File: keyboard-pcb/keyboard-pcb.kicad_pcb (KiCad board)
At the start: 2 copper layers, 57 parts, among them SW1 SW_Push, SW10 SW_Push, SW11 SW_Push, SW12 SW_Push, SW13 SW_Push, SW14 SW_Push, SW15 SW_Push, SW16 SW_Push, SW17 SW_Push, SW18 SW_Push, SW19 SW_Push, SW2 SW_Push, SW20 SW_Push, SW21 SW_Push, SW22 SW_Push, SW23 SW_Push, SW24 SW_Push, SW25 SW_Push, SW26 SW_Push, SW27 SW_Push, SW28 SW_Push, SW3 SW_Push, SW4 SW_Push, SW5 SW_Push, SW6 SW_Push, SW7 SW_Push, SW8 SW_Push, SW9 SW_Push, U1 RC1602A

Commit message: placement in progress
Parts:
- removed D28: 1N914, Diode_THT:D_DO-35_SOD27_P7.62mm_Horizontal
- removed SW28: SW_Push, Button_Switch_Keyboard:SW_Cherry_MX_1.00u_PCB
- added U1: ATmega328-P, Package_DIP:DIP-28_W7.62mm, F.Cu at (215.9, 52.1)
- D16, D20, D23, D7: moved to B.Cu
- moved SW24 169.6 mm to (102.9, 158.8)
- moved SW27 161.3 mm to (93.5, 178.4)
- moved D20 147.5 mm to (104.1, 154.3), turned to 180 degrees
- moved D23 146.3 mm to (85.1, 172.7), turned to 180 degrees
- moved SW22 146.3 mm to (64.8, 158.8)
- moved D16 140.7 mm to (104.1, 135.3), turned to 180 degrees
- moved SW26 126.6 mm to (64.8, 177.8)
- moved D7 123.0 mm to (85.1, 97.2), turned to 180 degrees
- moved SW23 122.6 mm to (83.8, 158.8)
- moved SW25 117.2 mm to (45.7, 177.8)
- renumbered U1 to U2
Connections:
- net Net-(D1-K) renamed /COL0
- net Net-(D10-K) renamed /COL1
- net Net-(D11-K) renamed /COL2
- net Net-(D12-K) renamed /COL3
- net Net-(SW1-Pad1) renamed /ROW0
- net Net-(SW10-Pad1) renamed /ROW2
- net Net-(SW13-Pad1) renamed /ROW3
- net Net-(SW17-Pad1) renamed /ROW4
- net Net-(SW21-Pad1) renamed /ROW5
- net Net-(SW25-Pad1) renamed /ROW6
- net Net-(SW5-Pad1) renamed /ROW1
- U2 pad 1: unconnected-(U1-VSS-Pad1) -> GND
- U2 pad 2: unconnected-(U1-VDD-Pad2) -> VCC
- U2 pad 5: unconnected-(U1-R/W-Pad5) -> GND

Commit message: placement
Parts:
- added R1: R, Resistor_THT:R_Axial_DIN0207_L6.3mm_D2.5mm_P7.62mm_Horizontal, B.Cu at (52.1, 53.3)
- added RV1: R_Potentiometer, Potentiometer_THT:Potentiometer_Bourns_3266P_Horizontal, B.Cu at (35.6, 40.6)
- U1: moved to B.Cu
- moved U1 128.7 mm to (87.6, 41.9), turned to 90 degrees
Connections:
- U2 pad 10: unconnected-(U2-DB3-Pad10) -> GND
- U2 pad 11: unconnected-(U2-DB4-Pad11) -> /D0
- U2 pad 12: unconnected-(U2-DB5-Pad12) -> /D1
- U2 pad 13: unconnected-(U2-DB6-Pad13) -> /D2
- U2 pad 14: unconnected-(U2-DB7-Pad14) -> /D3
- U2 pad 15: unconnected-(U2-A/VEE-Pad15) -> VCC
- U2 pad 16: unconnected-(U2-K-Pad16) -> Net-(U2-K)
- U2 pad 3: unconnected-(U2-VO-Pad3) -> Net-(U2-VO)
- U2 pad 4: unconnected-(U2-RS-Pad4) -> /RS
- U2 pad 6: unconnected-(U2-E-Pad6) -> /EN
- U2 pad 7: unconnected-(U2-DB0-Pad7) -> GND
- U2 pad 8: unconnected-(U2-DB1-Pad8) -> GND
- U2 pad 9: unconnected-(U2-DB2-Pad9) -> GND

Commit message: working on placement
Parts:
- added C1: 0.1uF, Capacitor_SMD:C_0805_2012Metric_Pad1.18x1.45mm_HandSolder, F.Cu at (129.3, 96.7)
- added C2: 10uF, Capacitor_SMD:C_0805_2012Metric_Pad1.18x1.45mm_HandSolder, F.Cu at (129.3, 99.7)
- added C3: 0.1uF, Capacitor_SMD:C_0805_2012Metric_Pad1.18x1.45mm_HandSolder, F.Cu at (129.3, 102.7)
- added D1: LED, LED_THT:LED_D3.0mm, F.Cu at (122.7, 81.7)
- added D11: LED, LED_THT:LED_D3.0mm, F.Cu at (122.7, 92.8)
- added D2: LED, LED_THT:LED_D3.0mm, F.Cu at (122.7, 87.3)
- added J1: Conn_02x03_Odd_Even, Connector_PinHeader_2.54mm:PinHeader_2x03_P2.54mm_Vertical, F.Cu at (140.0, 81.3)
- added R1: 470, Resistor_THT:R_Axial_DIN0207_L6.3mm_D2.5mm_P7.62mm_Horizontal, F.Cu at (128.5, 81.0)
- added R2: 470, Resistor_THT:R_Axial_DIN0207_L6.3mm_D2.5mm_P7.62mm_Horizontal, F.Cu at (128.5, 85.0)
- added R3: 470, Resistor_THT:R_Axial_DIN0207_L6.3mm_D2.5mm_P7.62mm_Horizontal, F.Cu at (128.5, 89.1)
- added R4: 10k, Resistor_THT:R_Axial_DIN0207_L6.3mm_D2.5mm_P7.62mm_Horizontal, F.Cu at (128.5, 93.1)
- added SW5: SW_SPST, Connector_PinHeader_2.54mm:PinHeader_1x02_P2.54mm_Vertical, F.Cu at (123.3, 97.9)
- added U1: R1500H, Package_TO_SOT_SMD:SOT-89-5_Handsoldering, F.Cu at (136.1, 98.2)
- R5: renamed from R1; value R -> 470
- RV1: value R_Potentiometer -> 10k
- renumbered D8 to D10, D9 to D12, D10 to D13, D11 to D14, D12 to D15, D13 to D16, D14 to D17, D15 to D18, D16 to D19, D17 to D20, D18 to D21, D19 to D22, D20 to D23, D21 to D24, D22 to D25, D23 to D26, D24 to D27, D25 to D28, D26 to D29, D1 to D3, D27 to D30, D2 to D4, D3 to D5, D4 to D6, D5 to D7, D6 to D8, D7 to D9, SW9 to SW10, SW10 to SW11, SW11 to SW12, SW12 to SW13, SW13 to SW14, SW14 to SW15, SW15 to SW16, SW16 to SW17, SW17 to SW18, SW18 to SW19, SW19 to SW20, SW20 to SW21, SW21 to SW22, SW22 to SW23, SW23 to SW24, SW24 to SW25, SW25 to SW26, SW26 to SW27, SW27 to SW28, SW5 to SW6, SW6 to SW7, SW7 to SW8, SW8 to SW9, U1 to U2, U2 to U3
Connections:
- U2 pad 14: unconnected-(U1-PB0-Pad14) -> Net-(D1-K)
- U2 pad 15: unconnected-(U1-PB1-Pad15) -> Net-(D2-K)

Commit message: starting software
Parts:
- added BT1: 2xAAA, Battery:BatteryHolder_Keystone_2468_2xAAA, F.Cu at (122.0, 131.0)
- C1: footprint Capacitor_SMD:C_0805_2012Metric_Pad1.18x1.45mm_HandSolder -> Capacitor_THT:C_Disc_D5.0mm_W2.5mm_P2.50mm; moved to B.Cu
- C2, C3: footprint Capacitor_SMD:C_0805_2012Metric_Pad1.18x1.45mm_HandSolder -> Capacitor_THT:C_Disc_D5.0mm_W2.5mm_P2.50mm
- D10, D12, D13, D14, D15, D16, D17, D18, D20, D21, D22, D24, D25, D27, D28, D29, D3, D30, D4, D5, D6, D7, D8: moved to B.Cu
- moved D27 155.1 mm to (104.1, 172.7), turned to 180 degrees
- moved D30 153.1 mm to (94.6, 193.0), turned to 180 degrees
- moved D6 152.9 mm to (104.1, 78.1), turned to 180 degrees
- moved D15 142.0 mm to (104.1, 116.2), turned to 180 degrees
- moved D10 141.3 mm to (104.1, 97.2), turned to 180 degrees
- moved D29 134.0 mm to (66.0, 192.4), turned to 180 degrees
- moved D5 133.5 mm to (85.1, 78.1), turned to 180 degrees
- moved D24 129.7 mm to (47.0, 173.4), turned to 180 degrees
- moved D22 129.6 mm to (85.1, 154.3), turned to 180 degrees
- moved D18 124.9 mm to (85.1, 135.3), turned to 180 degrees
- moved D25 124.9 mm to (66.0, 173.4), turned to 180 degrees
- moved D28 124.6 mm to (47.0, 192.4), turned to 180 degrees
- moved D14 123.9 mm to (85.1, 116.2), turned to 180 degrees
- moved D17 122.7 mm to (66.0, 135.3), turned to 180 degrees
- moved D20 119.6 mm to (47.0, 154.3), turned to 180 degrees
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
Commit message: placement done?
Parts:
- BT1, C2, C3, J1, U1: moved to B.Cu
- R5, U2: moved to F.Cu
- SW5: footprint Connector_PinHeader_2.54mm:PinHeader_1x02_P2.54mm_Vertical -> my_switch:ANT11TFHQE_switch; moved to B.Cu
- moved U1 120.1 mm to (35.4, 32.8), turned to 180 degrees
- moved C2 119.8 mm to (34.3, 26.7)
- moved C3 114.9 mm to (34.3, 38.1)
- moved BT1 114.7 mm to (47.2, 44.0)
- moved D1 88.3 mm to (37.5, 58.4)
- moved R1 87.6 mm to (43.8, 58.4)
- moved J1 77.2 mm to (92.7, 20.3), turned to -90 degrees
- moved R4 72.0 mm to (65.4, 58.4)
- moved SW5 66.3 mm to (100.2, 35.8), turned to 180 degrees
- moved R2 58.7 mm to (76.2, 58.4)
- moved R3 46.6 mm to (93.3, 58.4)
- moved D2 45.4 mm to (87.6, 58.4)
- moved D11 38.8 mm to (104.8, 58.4)
- moved U2 15.9 mm to (81.3, 27.3), turned to -90 degrees
- moved RV1 6.38 mm to (36.2, 47.0)
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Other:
- board outline added: 86.4 x 177.8 mm

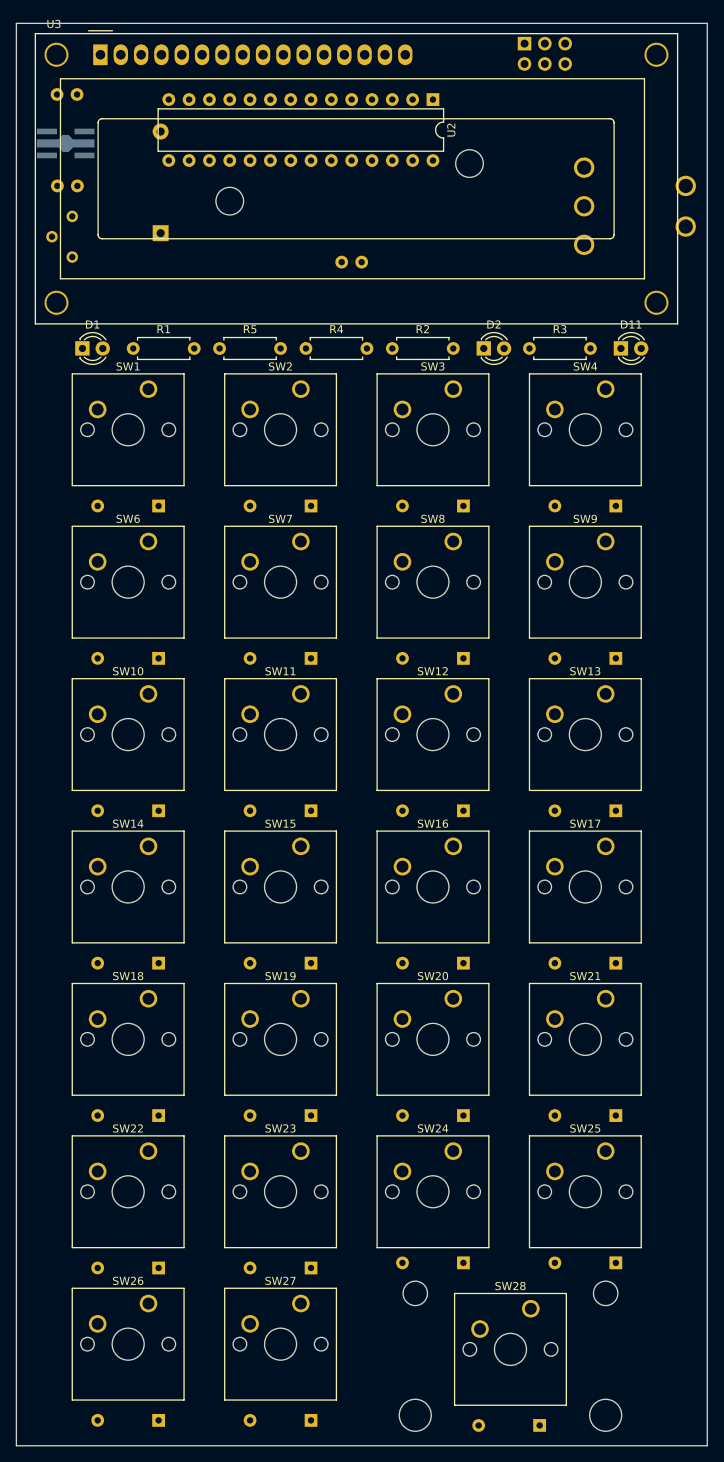
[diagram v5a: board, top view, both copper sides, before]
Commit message: change to AAA, software updates
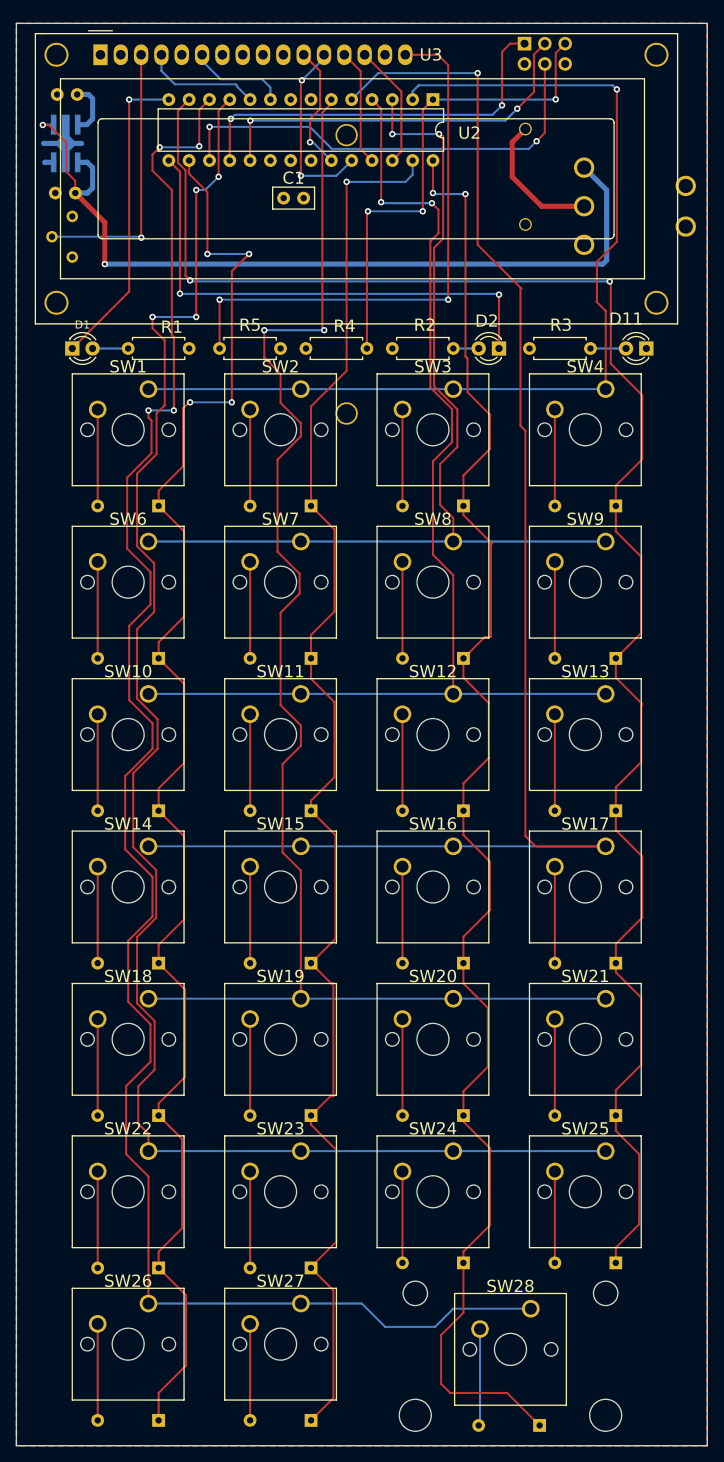
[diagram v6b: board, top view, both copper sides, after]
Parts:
- BT1: value 2xAAA -> 4xAAA; footprint Battery:BatteryHolder_Keystone_2468_2xAAA -> AAA_batt_holder:Keystone_4xAAA_2481
- C1: moved to F.Cu
- moved BT1 18.7 mm to (45.1, 25.4)
- moved C1 12.6 mm to (62.6, 39.6), turned to 0 degrees
- moved R1 6.98 mm to (50.8, 58.4), turned to 180 degrees
- moved D11 3.17 mm to (108.0, 58.4), turned to 180 degrees
- moved C2 2.52 mm to (36.8, 26.7), turned to 180 degrees
- moved C3 2.42 mm to (36.6, 39.0), turned to 180 degrees
- moved D2 1.91 mm to (89.5, 58.4), turned to 180 degrees
- moved D1 1.27 mm to (36.2, 58.4)
- turned U1 to 90 degrees
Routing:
- net /ROW6: track 0.00 -> 223.1 mm, vias 0 -> 4
- net /COL3: track 0.00 -> 215.2 mm, vias 0 -> 2
- net /ROW5: track 0.00 -> 207.1 mm, vias 0 -> 4
- net /COL2: track 0.00 -> 189.2 mm, vias 0 -> 2
- net /COL0: track 0.00 -> 187.3 mm, vias 0 -> 4
- net /ROW4: track 0.00 -> 185.8 mm, vias 0 -> 2
- net /ROW3: track 0.00 -> 182.8 mm, vias 0 -> 1
- net /COL1: track 0.00 -> 182.1 mm, vias 0 -> 1
- net /ROW2: track 0.00 -> 142.1 mm, vias 0 -> 2
- net /ROW0: track 0.00 -> 123.2 mm, vias 0 -> 1
- net /ROW1: track 0.00 -> 121.9 mm, vias 0 -> 2
- net Net-(SW5-A): track 0.00 -> 105.2 mm, vias 0 -> 2
- net Net-(U3-K): track 0.00 -> 69.9 mm, vias 0 -> 2
- net Net-(D2-K): track 0.00 -> 63.9 mm, vias 0 -> 2
- net /nRST: track 0.00 -> 61.4 mm, vias 0 -> 3
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- added copper zone on B.Cu, net GND
- added copper zone on F.Cu, net GND
- added copper zone on F.Cu, net VCC

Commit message: V1 ready to order?
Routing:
- net GND: track 5.84 -> 10.9 mm
- net /COL2: track 189.2 -> 188.8 mm, vias 2 -> 6
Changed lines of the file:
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@@
     (fp_arc (start 63.7 8) (mid 64.053553 8.146447) (end 64.2 8.5)
       (stroke (width 0.12) (type solid)) (layer "F.SilkS"))
-    (fp_arc (start 64.20104 22.49932) (mid 64.054479 22.85315) (end 63.70066 22.9997)
+    (fp_arc (start 64.20104 22.49932) (mid 64.054473 22.853115) (end 63.70066 22.9997)
       (stroke (width 0.12) (type solid)) (layer "F.SilkS"))
     (fp_line (start -8.25 -2.75) (end -8.25 33.75)
@@
   (segment (start 83.439 188.976) (end 90.551 188.976) (width 0.254) (layer "F.Cu") (net 30))
   (segment (start 85.09 78.105) (end 85.09 79.248) (width 0.254) (layer "F.Cu") (net 30))
+  (segment (start 88.646 91.059) (end 88.646 93.599) (width 0.254) (layer "F.Cu") (net 30))
   (segment (start 88.265 102.743) (end 85.09 99.568) (width 0.254) (layer "F.Cu") (net 30))
   (segment (start 88.392 70.993) (end 88.392 66.675) (width 0.254) (layer "F.Cu") (net 30))
@@
   (segment (start 85.09 112.776) (end 88.265 109.601) (width 0.254) (layer "F.Cu") (net 30))
   (segment (start 85.09 172.72) (end 85.09 171.323) (width 0.254) (layer "F.Cu") (net 30))
-  (segment (start 87.757 94.488) (end 85.09 97.155) (width 0.254) (layer "F.Cu") (net 30))
   (segment (start 85.09 151.257) (end 88.138 148.209) (width 0.254) (layer "F.Cu") (net 30))
   (segment (start 88.392 128.651) (end 88.392 122.555) (width 0.254) (layer "F.Cu") (net 30))
   (segment (start 85.09 135.255) (end 85.09 131.953) (width 0.254) (layer "F.Cu") (net 30))
-  (segment (start 88.519 94.488) (end 87.757 94.488) (width 0.254) (layer "F.Cu") (net 30))
   (segment (start 85.09 119.253) (end 85.09 116.205) (width 0.254) (layer "F.Cu") (net 30))
   (segment (start 85.09 137.795) (end 85.09 135.255) (width 0.254) (layer "F.Cu") (net 30))
@@
   (segment (start 88.265 109.601) (end 88.265 102.743) (width 0.254) (layer "F.Cu") (net 30))
   (segment (start 85.344 59.436) (end 85.344 39.116) (width 0.254) (layer "F.Cu") (net 30))
+  (segment (start 85.598 63.881) (end 86.36 64.643) (width 0.254) (layer "F.Cu") (net 30))
   (segment (start 81.28 38.989) (end 81.28 34.925) (width 0.254) (layer "F.Cu") (net 30))
   (segment (start 88.392 158.369) (end 85.09 155.067) (width 0.254) (layer "F.Cu") (net 30))
@@
   (segment (start 85.09 99.568) (end 85.09 97.155) (width 0.254) (layer "F.Cu") (net 30))
   (segment (start 82.296 181.737) (end 82.296 187.833) (width 0.254) (layer "F.Cu") (net 30))
-  (segment (start 88.646 82.804) (end 88.519 82.931) (width 0.254) (layer "F.Cu") (net 30))
-  (segment (start 88.519 82.931) (end 88.519 94.488) (width 0.254) (layer "F.Cu") (net 30))
+  (segment (start 88.646 82.804) (end 88.646 84.836) (width 0.254) (layer "F.Cu") (net 30))
   (segment (start 85.09 178.943) (end 82.296 181.737) (width 0.254) (layer "F.Cu") (net 30))
   (segment (start 85.09 131.953) (end 88.392 128.651) (width 0.254) (layer "F.Cu") (net 30))
@@
   (segment (start 85.09 154.305) (end 85.09 151.257) (width 0.254) (layer "F.Cu") (net 30))
   (segment (start 85.09 78.105) (end 85.09 74.295) (width 0.254) (layer "F.Cu") (net 30))
-  (segment (start 88.392 66.675) (end 85.598 63.881) (width 0.254) (layer "F.Cu") (net 30))
+  (segment (start 88.646 93.599) (end 85.09 97.155) (width 0.254) (layer "F.Cu") (net 30))
+  (segment (start 86.36 64.643) (end 86.487 64.643) (width 0.254) (layer "F.Cu") (net 30))
+  (via (at 88.646 91.059) (size 0.8) (drill 0.4) (layers "F.Cu" "B.Cu") (net 30))
   (via (at 81.28 38.989) (size 0.8) (drill 0.4) (layers "F.Cu" "B.Cu") (net 30))
+  (via (at 86.487 64.643) (size 0.8) (drill 0.4) (layers "F.Cu" "B.Cu") (net 30))
   (via (at 85.344 39.116) (size 0.8) (drill 0.4) (layers "F.Cu" "B.Cu") (net 30))
+  (via (at 88.646 84.836) (size 0.8) (drill 0.4) (layers "F.Cu" "B.Cu") (net 30))
+  (via (at 88.392 66.675) (size 0.8) (drill 0.4) (layers "F.Cu" "B.Cu") (net 30))
   (segment (start 85.344 39.116) (end 81.407 39.116) (width 0.254) (layer "B.Cu") (net 30))
+  (segment (start 86.487 64.643) (end 88.392 66.548) (width 0.254) (layer "B.Cu") (net 30))
   (segment (start 81.407 39.116) (end 81.28 38.989) (width 0.254) (layer "B.Cu") (net 30))
+  (segment (start 88.392 66.548) (end 88.392 66.675) (width 0.254) (layer "B.Cu") (net 30))
+  (segment (start 88.646 84.836) (end 88.646 91.059) (width 0.254) (layer "B.Cu") (net 30))
   (segment (start 104.14 99.568) (end 104.14 97.155) (width 0.254) (layer "F.Cu") (net 31))
   (segment (start 104.14 172.72) (end 104.14 170.815) (width 0.254) (layer "F.Cu") (net 31))
@@
   (segment (start 38.735 29.718) (end 38.735 27.178) (width 0.635) (layer "B.Cu") (net 40))
   (segment (start 36.87 30.44) (end 38.013 30.44) (width 0.635) (layer "B.Cu") (net 40))
+  (segment (start 65.111 39.624) (end 66.04 38.695) (width 0.25) (layer "F.Cu") (net 41))
+  (segment (start 66.04 38.695) (end 66.04 34.925) (width 0.25) (layer "F.Cu") (net 41))
   (segment (start 35.37 32.79) (end 32.663 32.79) (width 0.635) (layer "B.Cu") (net 41))
   (segment (start 33.87 35.14) (end 32.805 35.14) (width 0.635) (layer "B.Cu") (net 41))

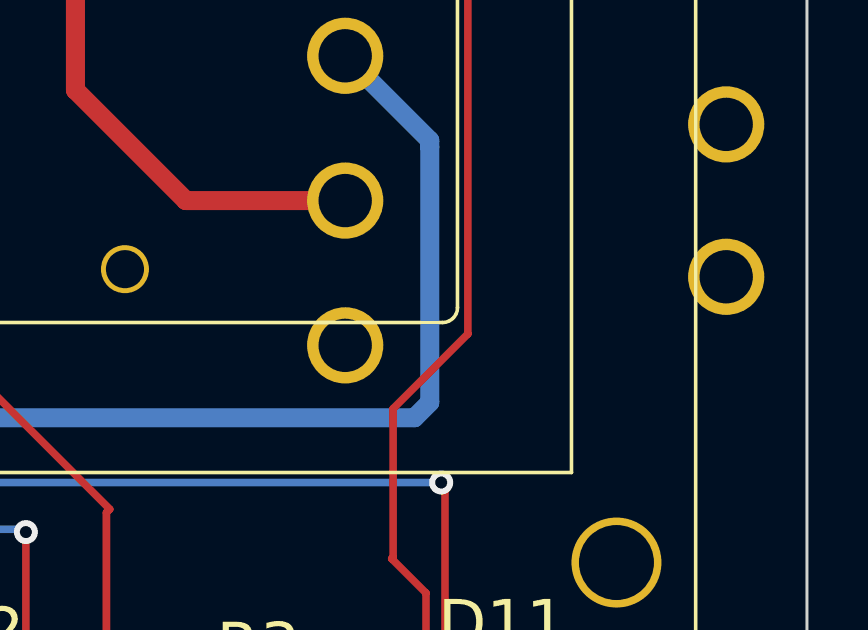
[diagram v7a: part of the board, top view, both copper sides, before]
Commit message: add 3D cherry model
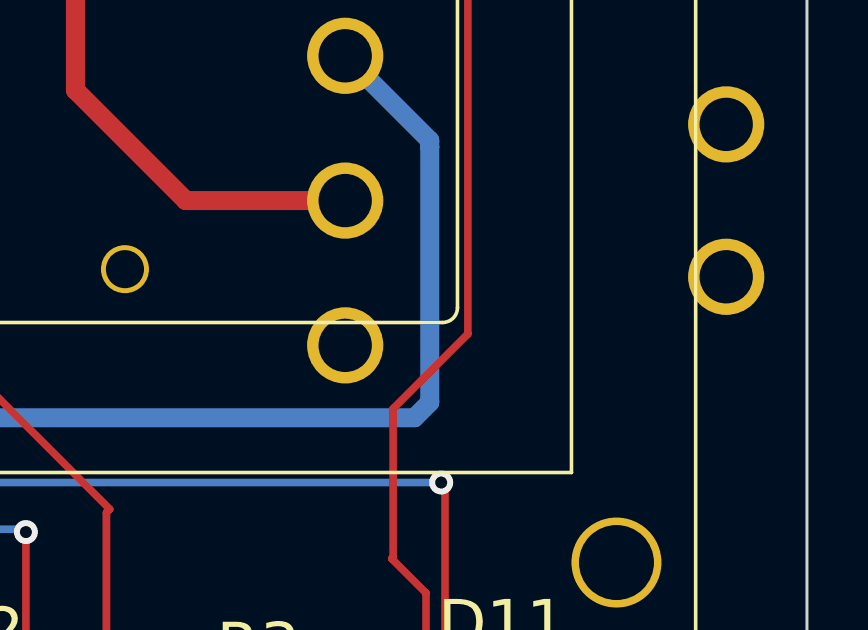
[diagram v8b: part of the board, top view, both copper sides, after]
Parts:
- SW1, SW10, SW11, SW12, SW13, SW14, SW15, SW16, SW17, SW18, SW19, SW2, SW20, SW21, SW22, SW23, SW24, SW25, SW26, SW27, SW3, SW4, SW6, SW7, SW8, SW9: footprint Button_Switch_Keyboard:SW_Cherry_MX_1.00u_PCB -> my_switch:SW_Cherry_MX_1.00u_PCB
